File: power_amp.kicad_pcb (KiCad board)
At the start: 2 copper layers, 100 x 70 mm, 59 parts, among them J1 Barrel_Jack_Switch, J2 Barrel_Jack_Switch, J3 Conn_Coaxial, J4 Conn_Coaxial, J5 AudioJack3_SwitchTR, J6 Conn_Coaxial, J7 Conn_Coaxial, Q1 Q_NPN_ECB, Q2 Q_PNP_ECB, Q3 Q_NPN_ECB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

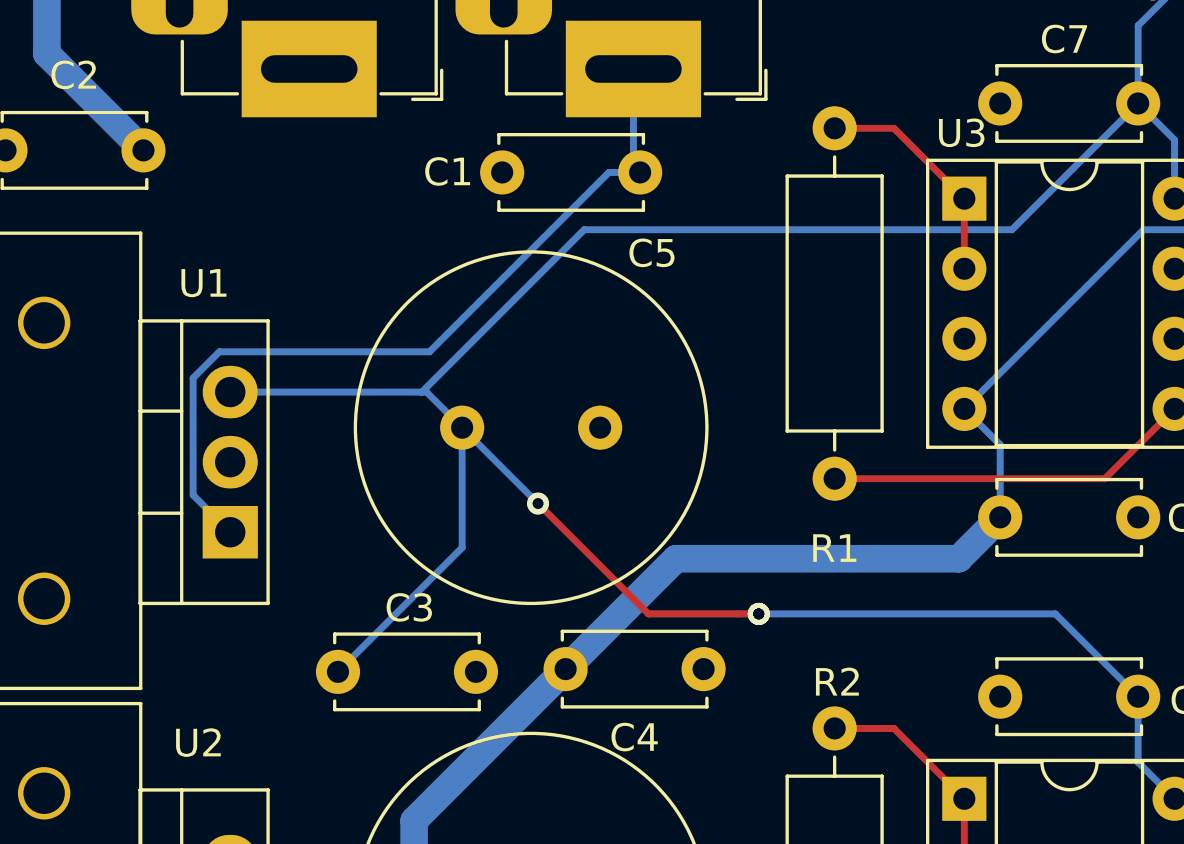
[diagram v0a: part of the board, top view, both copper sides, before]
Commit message: made power-line thick
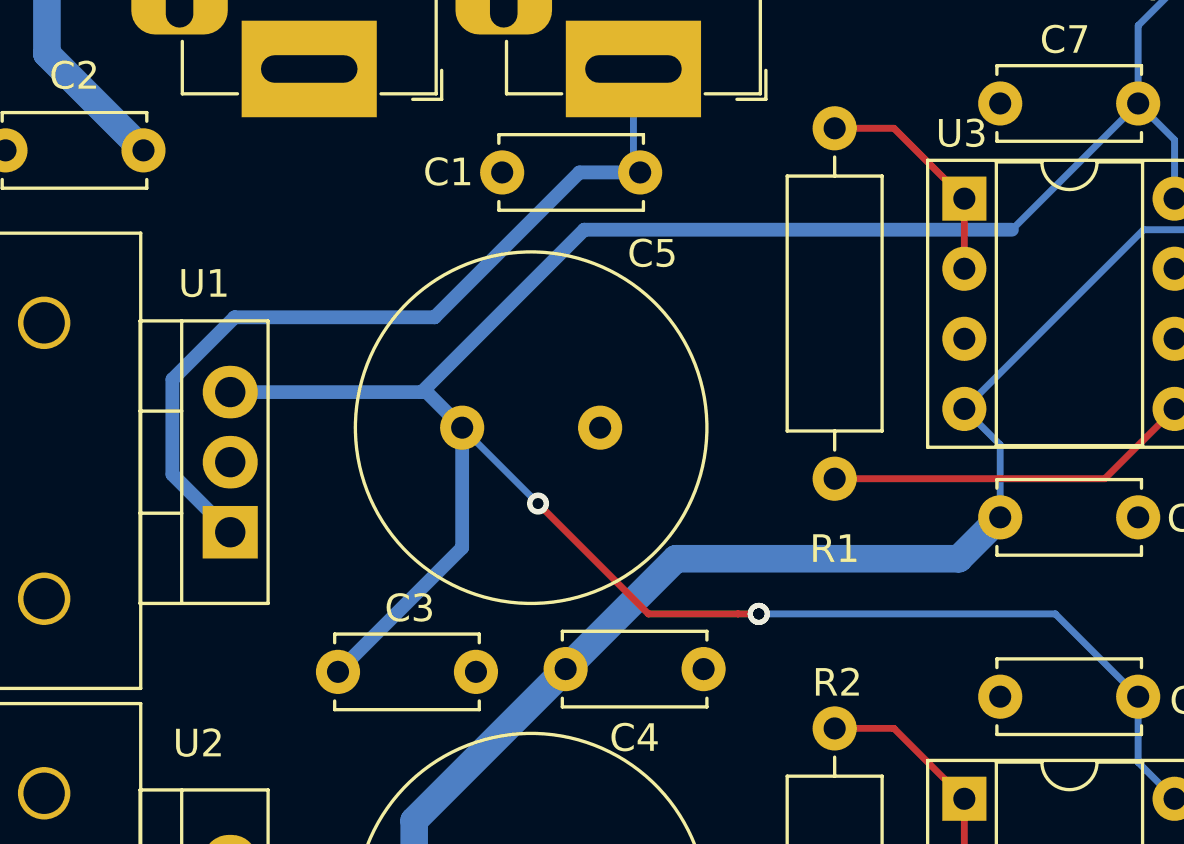
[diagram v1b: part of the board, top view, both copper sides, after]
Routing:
- net +6V: track 29.3 -> 30.3 mm
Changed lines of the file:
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@@
   (gr_line (start 71 134) (end 71 64) (layer "Edge.Cuts") (width 0.1))
   (gr_line (start 71 134) (end 171 134) (layer "Edge.Cuts") (width 0.1))
-  (segment (start 94.56863 82.5) (end 88.06863 89) (width 0.25) (layer "B.Cu") (net 1))
+  (segment (start 78.75 93.445) (end 80.845 95.54) (width 0.5) (layer "B.Cu") (net 1))
+  (segment (start 88.25 87.75) (end 81 87.75) (width 0.5) (layer "B.Cu") (net 1))
+  (segment (start 93.5 82.5) (end 88.25 87.75) (width 0.5) (layer "B.Cu") (net 1))
   (segment (start 95.4575 82.2575) (end 95.7 82.5) (width 0.25) (layer "B.Cu") (net 1))
-  (segment (start 95.7 82.5) (end 94.56863 82.5) (width 0.25) (layer "B.Cu") (net 1))
-  (segment (start 79.5 94.195) (end 80.845 95.54) (width 0.25) (layer "B.Cu") (net 1))
-  (segment (start 79.5 89.950842) (end 79.5 94.195) (width 0.25) (layer "B.Cu") (net 1))
-  (segment (start 88.06863 89) (end 80.450842 89) (width 0.25) (layer "B.Cu") (net 1))
-  (segment (start 80.450842 89) (end 79.5 89.950842) (width 0.25) (layer "B.Cu") (net 1))
+  (segment (start 81 87.75) (end 78.75 90) (width 0.5) (layer "B.Cu") (net 1))
+  (segment (start 95.7 82.5) (end 93.5 82.5) (width 0.5) (layer "B.Cu") (net 1))
+  (segment (start 78.75 90) (end 78.75 93.445) (width 0.5) (layer "B.Cu") (net 1))
   (segment (start 95.4575 78.75) (end 95.4575 82.2575) (width 0.25) (layer "B.Cu") (net 1))
   (segment (start 130.5 75) (end 130.5 80.55) (width 0.25) (layer "F.Cu") (net 3))
@@
   (segment (start 131.499999 124.500001) (end 130 126) (width 0.25) (layer "B.Cu") (net 3))
   (segment (start 115.07 81.32) (end 113.75 80) (width 0.25) (layer "B.Cu") (net 3))
-  (segment (start 87.79 90.46) (end 93.675 84.575) (width 0.25) (layer "B.Cu") (net 3))
+  (segment (start 87.79 90.46) (end 93.675 84.575) (width 0.5) (layer "B.Cu") (net 3))
   (segment (start 140.875 127.475) (end 142.1 126.25) (width 0.25) (layer "B.Cu") (net 3))
   (segment (start 128.525 127.475) (end 130 126) (width 0.25) (layer "B.Cu") (net 3))
@@
   (segment (start 113.75 103.88) (end 115.07 105.2) (width 0.25) (layer "B.Cu") (net 3))
   (segment (start 119.8 71.925) (end 121.025 73.15) (width 0.25) (layer "B.Cu") (net 3))
-  (segment (start 80.845 90.46) (end 87.79 90.46) (width 0.25) (layer "B.Cu") (net 3))
+  (segment (start 80.845 90.46) (end 87.79 90.46) (width 0.5) (layer "B.Cu") (net 3))
   (segment (start 110.75 98.5) (end 113.75 101.5) (width 0.25) (layer "B.Cu") (net 3))
   (segment (start 126.55 73.15) (end 126.7 73) (width 0.25) (layer "B.Cu") (net 3))
@@
   (segment (start 121.025 73.15) (end 126.55 73.15) (width 0.25) (layer "B.Cu") (net 3))
   (segment (start 89.25 91.75) (end 92 94.5) (width 0.25) (layer "B.Cu") (net 3))
-  (segment (start 87.79 90.46) (end 87.96 90.46) (width 0.25) (layer "B.Cu") (net 3))
   (segment (start 113.75 101.5) (end 113.75 103.88) (width 0.25) (layer "B.Cu") (net 3))
   (segment (start 130.7 115.35) (end 131.499999 116.149999) (width 0.25) (layer "B.Cu") (net 3))
   (segment (start 100 98.5) (end 110.75 98.5) (width 0.25) (layer "B.Cu") (net 3))
-  (segment (start 89.25 91.75) (end 89.25 96.1) (width 0.25) (layer "B.Cu") (net 3))
+  (segment (start 89.25 91.75) (end 89.25 96.1) (width 0.5) (layer "B.Cu") (net 3))
   (segment (start 109.175 84.575) (end 113.75 80) (width 0.25) (layer "B.Cu") (net 3))
   (segment (start 126.7 73) (end 128.5 73) (width 0.25) (layer "B.Cu") (net 3))
   (segment (start 128.5 73) (end 130.5 75) (width 0.25) (layer "B.Cu") (net 3))
-  (segment (start 87.96 90.46) (end 89.25 91.75) (width 0.25) (layer "B.Cu") (net 3))
+  (segment (start 87.96 90.46) (end 89.25 91.75) (width 0.5) (layer "B.Cu") (net 3))
   (segment (start 115.07 83.45) (end 115.07 81.32) (width 0.25) (layer "B.Cu") (net 3))
   (segment (start 137.775 70.7) (end 139 71.925) (width 0.25) (layer "B.Cu") (net 3))
@@
   (segment (start 130 126) (end 131.475 127.475) (width 0.25) (layer "B.Cu") (net 3))
   (segment (start 119.002588 71.925) (end 119.8 71.925) (width 0.25) (layer "B.Cu") (net 3))
-  (segment (start 93.675 84.575) (end 109.175 84.575) (width 0.25) (layer "B.Cu") (net 3))
-  (segment (start 89.25 96.1) (end 84.75 100.6) (width 0.25) (layer "B.Cu") (net 3))
+  (segment (start 93.675 84.575) (end 109.175 84.575) (width 0.5) (layer "B.Cu") (net 3))
+  (segment (start 89.25 96.1) (end 84.75 100.6) (width 0.5) (layer "B.Cu") (net 3))
   (segment (start 83.7075 72.75) (end 76.35 72.75) (width 1) (layer "B.Cu") (net 4))
   (segment (start 74.2 78.2) (end 77.7 81.7) (width 1) (layer "B.Cu") (net 4))
